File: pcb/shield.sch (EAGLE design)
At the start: 10 parts, among them IC2 7805DT, U1 ARDUINO_SHIELDLABEL

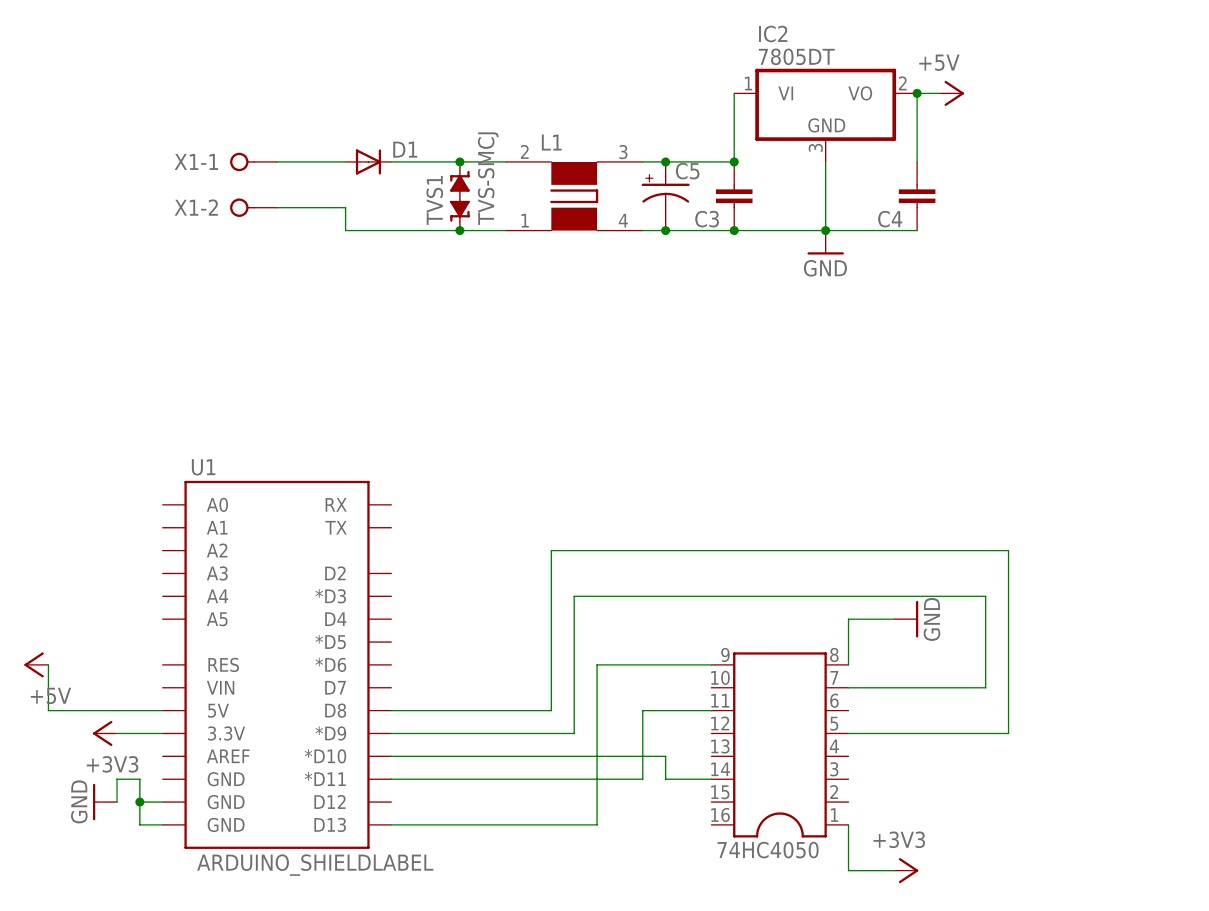
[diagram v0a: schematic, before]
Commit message: moved the source and added pinheader for the display
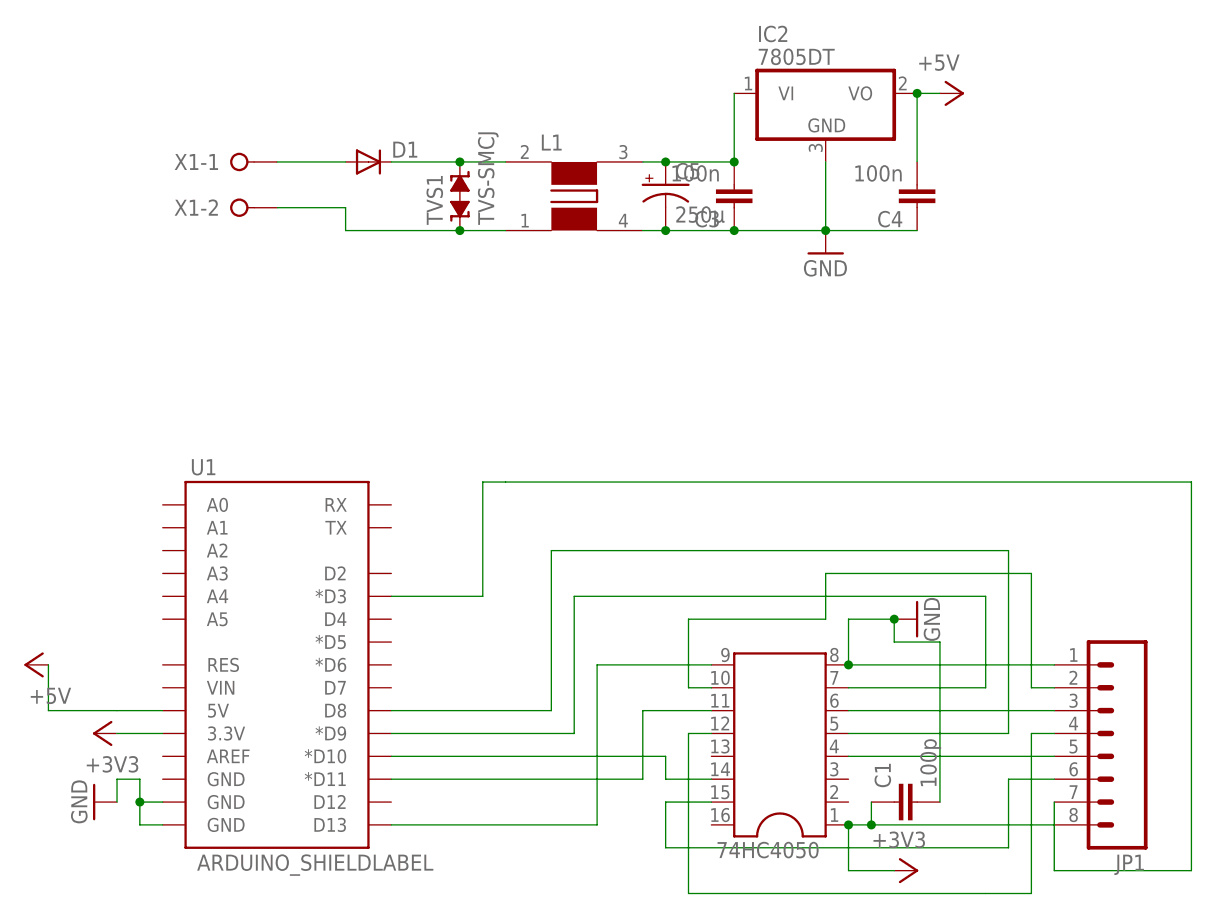
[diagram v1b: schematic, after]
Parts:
- added C1: 100p, rcl:C-EUC0603K
- added JP1: (no value), SparkFun:M083.5MM-8
- C3, C4: value (none) -> 100n
- C5: value (none) -> 250µ
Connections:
- new net N$11: 74HC4050.6, JP1.3
- new net N$12: 74HC4050.12, JP1.4
- new net N$13: 74HC4050.4, JP1.5
- new net N$14: 74HC4050.15, JP1.6
- new net N$15: JP1.7, U1.*D3
- new net N$8: 74HC4050.10, JP1.2
- net +3V3: now also C1.1, JP1.8
- net GND: now also C1.2, JP1.1
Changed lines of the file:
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@@
 <part name="+3V2" library="supply1" deviceset="+3V3" device=""/>
 <part name="GND3" library="supply1" deviceset="GND" device=""/>
-<part name="C3" library="rcl" deviceset="C-EU" device="C1206K"/>
-<part name="C4" library="rcl" deviceset="C-EU" device="C1206K"/>
-<part name="C5" library="SparkFun" deviceset="CAP_POL" device="H13"/>
+<part name="C3" library="rcl" deviceset="C-EU" device="C1206K" value="100n"/>
+<part name="C4" library="rcl" deviceset="C-EU" device="C1206K" value="100n"/>
+<part name="C5" library="SparkFun" deviceset="CAP_POL" device="H13" value="250µ"/>
 <part name="L1" library="wuerth-elektronik" deviceset="WE-SL2" device=""/>
 <part name="TVS1" library="supressor" deviceset="TVS-" device="SMCJ"/>
 <part name="D1" library="diode" deviceset="DIODE-" device="DO-214AC"/>
 <part name="X1" library="con-wago-508" deviceset="W237-02P" device=""/>
+<part name="JP1" library="SparkFun" deviceset="M08" device="3.5MM-8"/>
+<part name="C1" library="rcl" deviceset="C-EU" device="C0603K" value="100p"/>
 </parts>
 <sheets>
@@
 <instance part="X1" gate="-1" x="78.74" y="111.76"/>
 <instance part="X1" gate="-2" x="78.74" y="106.68"/>
+<instance part="JP1" gate="G$1" x="175.26" y="48.26" rot="R180"/>
+<instance part="C1" gate="G$1" x="152.4" y="40.64" rot="R90"/>
 </instances>
 <busses>
@@
 <wire x1="152.4" y1="60.96" x2="147.32" y2="60.96" width="0.1524" layer="91"/>
 <wire x1="147.32" y1="60.96" x2="147.32" y2="55.88" width="0.1524" layer="91"/>
+<pinref part="JP1" gate="G$1" pin="1"/>
+<wire x1="147.32" y1="55.88" x2="170.18" y2="55.88" width="0.1524" layer="91"/>
+<junction x="147.32" y="55.88"/>
+<pinref part="C1" gate="G$1" pin="2"/>
+<wire x1="157.48" y1="40.64" x2="157.48" y2="58.42" width="0.1524" layer="91"/>
+<wire x1="157.48" y1="58.42" x2="152.4" y2="58.42" width="0.1524" layer="91"/>
+<wire x1="152.4" y1="58.42" x2="152.4" y2="60.96" width="0.1524" layer="91"/>
+<junction x="152.4" y="60.96"/>
 </segment>
 <segment>
@@
 <wire x1="147.32" y1="33.02" x2="147.32" y2="38.1" width="0.1524" layer="91"/>
 <pinref part="+3V1" gate="G$1" pin="+3V3"/>
+<pinref part="JP1" gate="G$1" pin="8"/>
+<wire x1="147.32" y1="38.1" x2="149.86" y2="38.1" width="0.1524" layer="91"/>
+<junction x="147.32" y="38.1"/>
+<pinref part="C1" gate="G$1" pin="1"/>
+<wire x1="149.86" y1="38.1" x2="170.18" y2="38.1" width="0.1524" layer="91"/>
+<wire x1="149.86" y1="40.64" x2="149.86" y2="38.1" width="0.1524" layer="91"/>
+<junction x="149.86" y="38.1"/>
 </segment>
 <segment>
@@
 </segment>
 </net>
+<net name="N$8" class="0">
+<segment>
+<pinref part="74HC4050" gate="G$1" pin="10"/>
+<wire x1="132.08" y1="53.34" x2="129.54" y2="53.34" width="0.1524" layer="91"/>
+<wire x1="129.54" y1="53.34" x2="129.54" y2="60.96" width="0.1524" layer="91"/>
+<wire x1="129.54" y1="60.96" x2="144.78" y2="60.96" width="0.1524" layer="91"/>
+<wire x1="144.78" y1="60.96" x2="144.78" y2="66.04" width="0.1524" layer="91"/>
+<wire x1="144.78" y1="66.04" x2="167.64" y2="66.04" width="0.1524" layer="91"/>
+<wire x1="167.64" y1="66.04" x2="167.64" y2="53.34" width="0.1524" layer="91"/>
+<pinref part="JP1" gate="G$1" pin="2"/>
+<wire x1="167.64" y1="53.34" x2="170.18" y2="53.34" width="0.1524" layer="91"/>
+</segment>
+</net>
+<net name="N$11" class="0">
+<segment>
+<pinref part="74HC4050" gate="G$1" pin="6"/>
+<pinref part="JP1" gate="G$1" pin="3"/>
+<wire x1="147.32" y1="50.8" x2="170.18" y2="50.8" width="0.1524" layer="91"/>
+</segment>
+</net>
+<net name="N$12" class="0">
+<segment>
+<pinref part="74HC4050" gate="G$1" pin="12"/>
+<wire x1="132.08" y1="48.26" x2="129.54" y2="48.26" width="0.1524" layer="91"/>
+<wire x1="129.54" y1="48.26" x2="129.54" y2="30.48" width="0.1524" layer="91"/>
+<wire x1="129.54" y1="30.48" x2="162.56" y2="30.48" width="0.1524" layer="91"/>
+<wire x1="162.56" y1="30.48" x2="167.64" y2="30.48" width="0.1524" layer="91"/>
+<wire x1="167.64" y1="30.48" x2="167.64" y2="48.26" width="0.1524" layer="91"/>
+<pinref part="JP1" gate="G$1" pin="4"/>
+<wire x1="167.64" y1="48.26" x2="170.18" y2="48.26" width="0.1524" layer="91"/>
+</segment>
+</net>
+<net name="N$13" class="0">
+<segment>
+<pinref part="74HC4050" gate="G$1" pin="4"/>
+<pinref part="JP1" gate="G$1" pin="5"/>
+<wire x1="147.32" y1="45.72" x2="170.18" y2="45.72" width="0.1524" layer="91"/>
+</segment>
+</net>
+<net name="N$14" class="0">
+<segment>
+<pinref part="74HC4050" gate="G$1" pin="15"/>
+<wire x1="132.08" y1="40.64" x2="127" y2="40.64" width="0.1524" layer="91"/>
+<wire x1="127" y1="40.64" x2="127" y2="35.56" width="0.1524" layer="91"/>
+<wire x1="127" y1="35.56" x2="165.1" y2="35.56" width="0.1524" layer="91"/>
+<wire x1="165.1" y1="35.56" x2="165.1" y2="43.18" width="0.1524" layer="91"/>
+<pinref part="JP1" gate="G$1" pin="6"/>
+<wire x1="165.1" y1="43.18" x2="170.18" y2="43.18" width="0.1524" layer="91"/>
+</segment>
+</net>
+<net name="N$15" class="0">
+<segment>
+<pinref part="JP1" gate="G$1" pin="7"/>
+<wire x1="170.18" y1="40.64" x2="170.18" y2="33.02" width="0.1524" layer="91"/>
+<wire x1="170.18" y1="33.02" x2="185.42" y2="33.02" width="0.1524" layer="91"/>
+<wire x1="185.42" y1="33.02" x2="185.42" y2="76.2" width="0.1524" layer="91"/>
+<wire x1="185.42" y1="76.2" x2="109.22" y2="76.2" width="0.1524" layer="91"/>
+<wire x1="109.22" y1="76.2" x2="106.68" y2="76.2" width="0.1524" layer="91"/>
+<wire x1="106.68" y1="76.2" x2="106.68" y2="63.5" width="0.1524" layer="91"/>
+<pinref part="U1" gate="G$1" pin="*D3"/>
+<wire x1="106.68" y1="63.5" x2="96.52" y2="63.5" width="0.1524" layer="91"/>
+</segment>
+</net>
